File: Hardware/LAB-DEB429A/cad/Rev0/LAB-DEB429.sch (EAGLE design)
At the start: 102 parts, among them J1 TSW-132-02-S-D, J2 TSW-132-02-S-D, U1 LAB-ADSM300F, U10 SF-MICROSD, U11 25MPX, U12 LAB-PPS330D, U13 LAB-PPS330D, U14 LAB-PPS330D, U15 SI1143, U16 LAB-PPS330D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

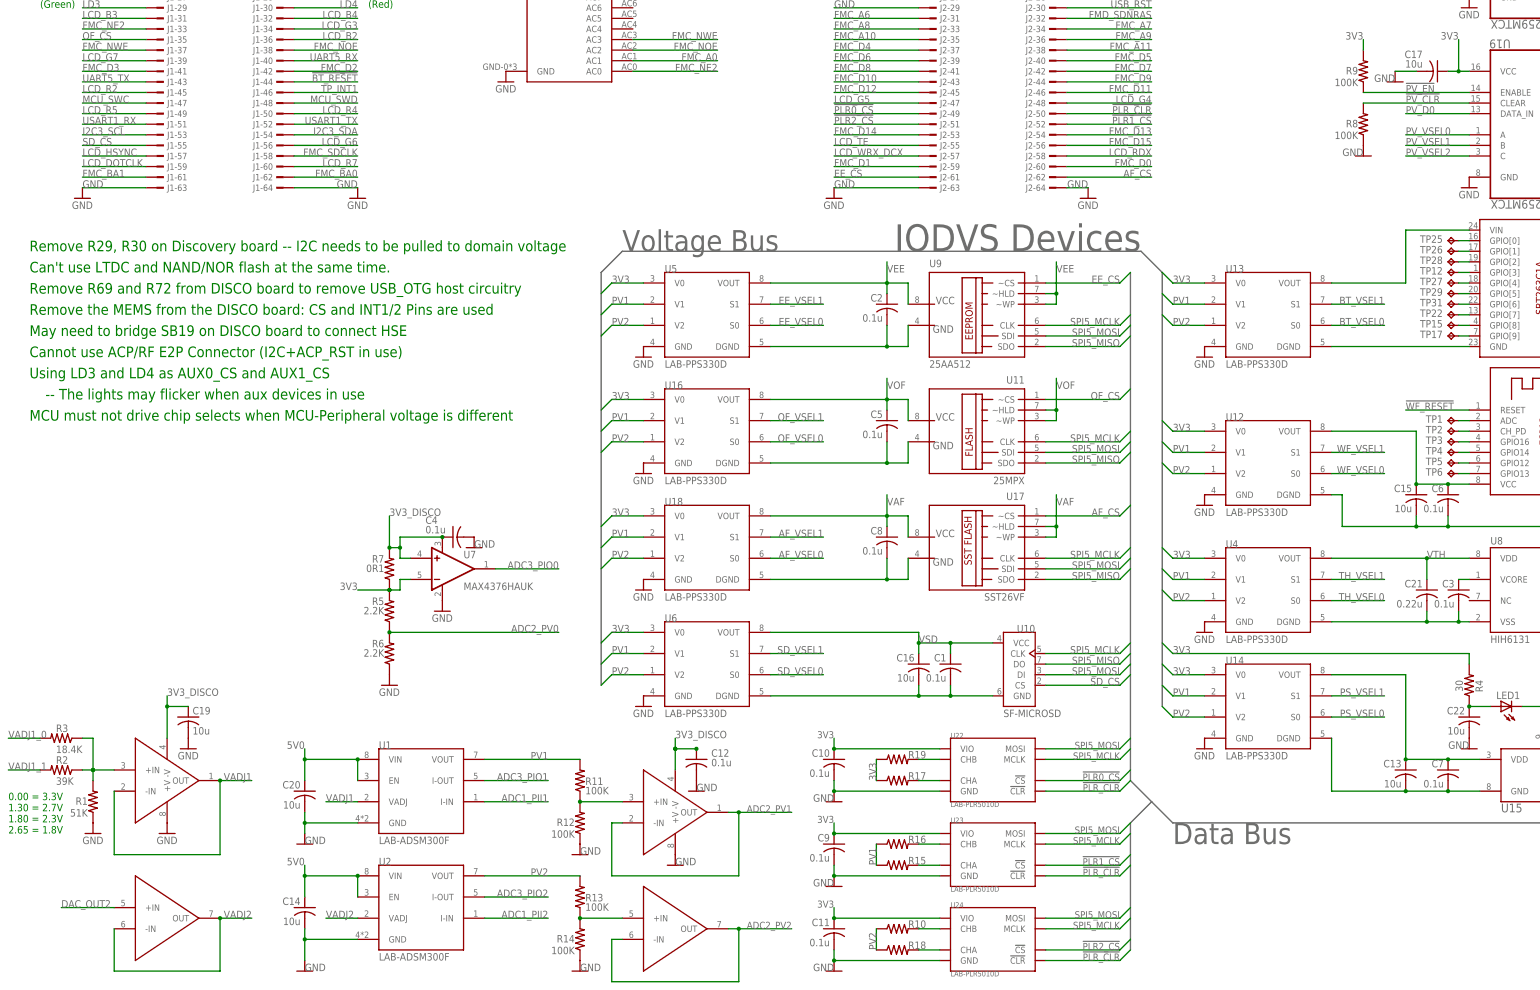
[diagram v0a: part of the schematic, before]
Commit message: 1) Updating the BOMs to synchronize purchasing.
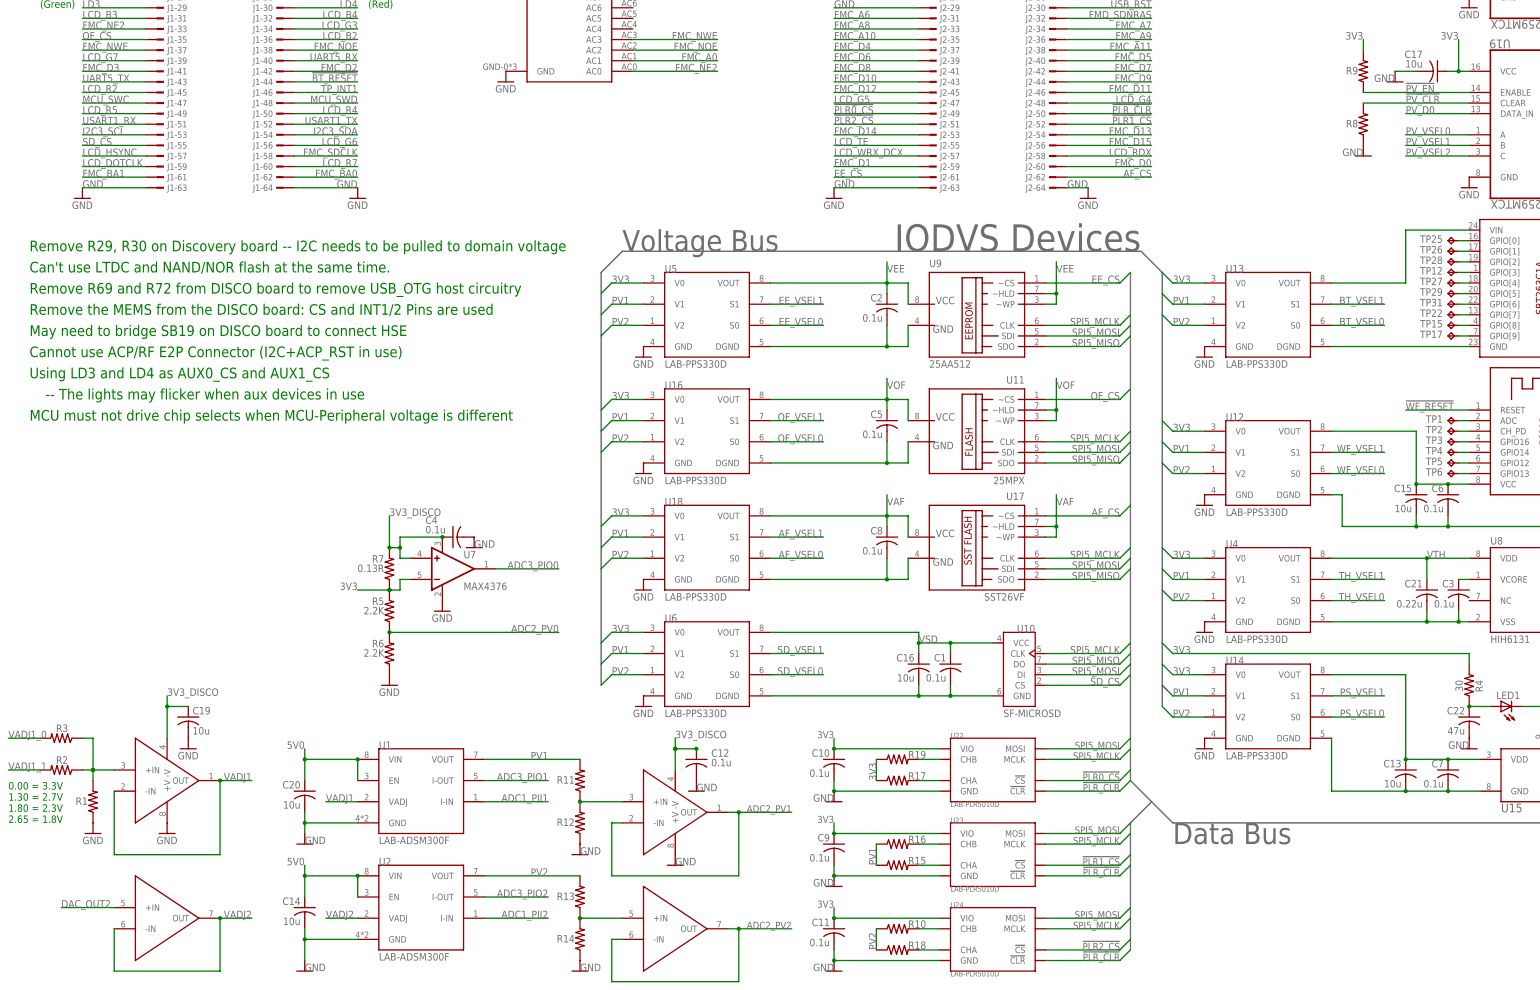
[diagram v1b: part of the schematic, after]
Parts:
- C22: value 10u -> 47u
- R1: value 51K -> (none)
- R11, R12, R13, R14, R8, R9: value 100K -> (none)
- R2: value 39K -> (none)
- R3: value 18.4K -> (none)
- R7: value 0R1 -> 0.13R
- U7: value MAX4376HAUK -> MAX4376
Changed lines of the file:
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@@
 <part name="C19" library="rcl" deviceset="C-US" device="C0603" value="10u"/>
 <part name="GND17" library="SparkFun-Aesthetics" deviceset="GND" device=""/>
-<part name="R1" library="rcl" deviceset="R-US_" device="R0603" value="51K"/>
+<part name="R1" library="rcl" deviceset="R-US_" device="R0603"/>
 <part name="GND18" library="SparkFun-Aesthetics" deviceset="GND" device=""/>
-<part name="R2" library="rcl" deviceset="R-US_" device="R0603" value="39K"/>
-<part name="R3" library="rcl" deviceset="R-US_" device="R0603" value="18.4K"/>
+<part name="R2" library="rcl" deviceset="R-US_" device="R0603"/>
+<part name="R3" library="rcl" deviceset="R-US_" device="R0603"/>
 <part name="U25" library="adafruit" deviceset="ESP-12" device=""/>
 <part name="U12" library="LAB304" deviceset="LAB-PPS330D" device=""/>
@@
 <part name="C13" library="rcl" deviceset="C-US" device="C0603" value="10u"/>
 <part name="GND2" library="SparkFun-Aesthetics" deviceset="GND" device=""/>
-<part name="C22" library="rcl" deviceset="C-US" device="C0603" value="10u"/>
+<part name="C22" library="rcl" deviceset="C-US" device="C0603" value="47u"/>
 <part name="GND3" library="SparkFun-Aesthetics" deviceset="GND" device=""/>
 <part name="U4" library="LAB304" deviceset="LAB-PPS330D" device=""/>
@@
 <part name="R6" library="rcl" deviceset="R-US_" device="R0603" value="2.2K"/>
 <part name="GND7" library="SparkFun-Aesthetics" deviceset="GND" device=""/>
-<part name="U7" library="PEGMA" deviceset="MAX4376" device="" value="MAX4376HAUK"/>
-<part name="R7" library="rcl" deviceset="R-US_" device="R0603" value="0R1"/>
+<part name="U7" library="PEGMA" deviceset="MAX4376" device=""/>
+<part name="R7" library="rcl" deviceset="R-US_" device="R0603" value="0.13R"/>
 <part name="GND8" library="SparkFun-Aesthetics" deviceset="GND" device=""/>
 <part name="C4" library="rcl" deviceset="C-US" device="C0603" value="0.1u"/>
@@
 <part name="C18" library="rcl" deviceset="C-US" device="C0603" value="10u"/>
 <part name="GND23" library="SparkFun-Aesthetics" deviceset="GND" device=""/>
-<part name="R8" library="rcl" deviceset="R-US_" device="R0603" value="100K"/>
+<part name="R8" library="rcl" deviceset="R-US_" device="R0603"/>
 <part name="GND24" library="SparkFun-Aesthetics" deviceset="GND" device=""/>
-<part name="R9" library="rcl" deviceset="R-US_" device="R0603" value="100K"/>
+<part name="R9" library="rcl" deviceset="R-US_" device="R0603"/>
 <part name="GND27" library="SparkFun-Aesthetics" deviceset="GND" device=""/>
 <part name="GND28" library="SparkFun-Aesthetics" deviceset="GND" device=""/>
@@
 <part name="C10" library="rcl" deviceset="C-US" device="C0603" value="0.1u"/>
 <part name="GND33" library="SparkFun-Aesthetics" deviceset="GND" device=""/>
-<part name="R11" library="rcl" deviceset="R-US_" device="R0603" value="100K"/>
-<part name="R12" library="rcl" deviceset="R-US_" device="R0603" value="100K"/>
-<part name="R13" library="rcl" deviceset="R-US_" device="R0603" value="100K"/>
-<part name="R14" library="rcl" deviceset="R-US_" device="R0603" value="100K"/>
+<part name="R11" library="rcl" deviceset="R-US_" device="R0603"/>
+<part name="R12" library="rcl" deviceset="R-US_" device="R0603"/>
+<part name="R13" library="rcl" deviceset="R-US_" device="R0603"/>
+<part name="R14" library="rcl" deviceset="R-US_" device="R0603"/>
 <part name="GND34" library="SparkFun-Aesthetics" deviceset="GND" device=""/>
 <part name="GND35" library="SparkFun-Aesthetics" deviceset="GND" device=""/>
@@
 <text x="10.16" y="172.72" size="2.54" layer="91">Can't use LTDC and NAND/NOR flash at the same time.</text>
 <text x="10.16" y="167.64" size="2.54" layer="91">Remove R69 and R72 from DISCO board to remove USB_OTG host circuitry</text>
-<text x="5.08" y="38.1" size="1.778" layer="91">0.00 = 3.3V
+<text x="5.08" y="40.64" size="1.778" layer="91">0.00 = 3.3V
 1.30 = 2.7V
 1.80 = 2.3V
@@
 <instance part="R1" gate="G$1" x="25.4" y="45.72" smashed="yes" rot="R90">
 <attribute name="NAME" x="24.13" y="46.7614" size="1.778" layer="95" rot="R180"/>
-<attribute name="VALUE" x="24.13" y="43.942" size="1.778" layer="96" rot="R180"/>
+<attribute name="VALUE" x="28.702" y="41.91" size="1.778" layer="96" rot="R90"/>
 </instance>
 <instance part="GND18" gate="1" x="25.4" y="38.1"/>
 <instance part="R2" gate="G$1" x="17.78" y="53.34" smashed="yes" rot="R180">
 <attribute name="NAME" x="16.51" y="54.8386" size="1.778" layer="95"/>
-<attribute name="VALUE" x="16.51" y="51.562" size="1.778" layer="96" rot="MR180"/>
+<attribute name="VALUE" x="21.59" y="56.642" size="1.778" layer="96" rot="R180"/>
 </instance>
 <instance part="R3" gate="G$1" x="17.78" y="60.96" smashed="yes" rot="R180">
 <attribute name="NAME" x="16.51" y="62.4586" size="1.778" layer="95"/>
-<attribute name="VALUE" x="16.51" y="59.182" size="1.778" layer="96" rot="MR180"/>
+<attribute name="VALUE" x="21.59" y="64.262" size="1.778" layer="96" rot="R180"/>
 </instance>
 <instance part="U25" gate="G$1" x="373.38" y="134.62"/>
@@
 <instance part="R8" gate="G$1" x="330.2" y="208.28" smashed="yes" rot="R90">
 <attribute name="NAME" x="328.93" y="209.3214" size="1.778" layer="95" rot="R180"/>
-<attribute name="VALUE" x="328.93" y="206.502" size="1.778" layer="96" rot="R180"/>
+<attribute name="VALUE" x="333.502" y="204.47" size="1.778" layer="96" rot="R90"/>
 </instance>
 <instance part="GND24" gate="1" x="330.2" y="200.66" smashed="yes">
@@
 <instance part="R9" gate="G$1" x="330.2" y="220.98" smashed="yes" rot="R90">
 <attribute name="NAME" x="328.93" y="222.0214" size="1.778" layer="95" rot="R180"/>
-<attribute name="VALUE" x="328.93" y="219.202" size="1.778" layer="96" rot="R180"/>
+<attribute name="VALUE" x="333.502" y="217.17" size="1.778" layer="96" rot="R90"/>
 </instance>
 <instance part="GND27" gate="1" x="88.9" y="190.5"/>
@@
 </instance>
 <instance part="R11" gate="G$1" x="142.24" y="50.8" smashed="yes" rot="R90">
-<attribute name="NAME" x="143.51" y="49.7586" size="1.778" layer="95"/>
-<attribute name="VALUE" x="143.51" y="47.498" size="1.778" layer="96"/>
+<attribute name="NAME" x="140.97" y="51.8414" size="1.778" layer="95" rot="R180"/>
+<attribute name="VALUE" x="145.542" y="46.99" size="1.778" layer="96" rot="R90"/>
 </instance>
 <instance part="R12" gate="G$1" x="142.24" y="40.64" smashed="yes" rot="R90">
 <attribute name="NAME" x="140.97" y="41.6814" size="1.778" layer="95" rot="R180"/>
-<attribute name="VALUE" x="140.97" y="38.862" size="1.778" layer="96" rot="R180"/>
+<attribute name="VALUE" x="145.542" y="36.83" size="1.778" layer="96" rot="R90"/>
 </instance>
 <instance part="R13" gate="G$1" x="142.24" y="22.86" smashed="yes" rot="R90">
-<attribute name="NAME" x="143.51" y="21.8186" size="1.778" layer="95"/>
-<attribute name="VALUE" x="143.51" y="19.558" size="1.778" layer="96"/>
+<attribute name="NAME" x="140.97" y="23.9014" size="1.778" layer="95" rot="R180"/>
+<attribute name="VALUE" x="145.542" y="19.05" size="1.778" layer="96" rot="R90"/>
 </instance>
 <instance part="R14" gate="G$1" x="142.24" y="12.7" smashed="yes" rot="R90">
 <attribute name="NAME" x="140.97" y="13.7414" size="1.778" layer="95" rot="R180"/>
-<attribute name="VALUE" x="140.97" y="10.922" size="1.778" layer="96" rot="R180"/>
+<attribute name="VALUE" x="145.542" y="8.89" size="1.778" layer="96" rot="R90"/>
 </instance>
 <instance part="GND34" gate="1" x="142.24" y="33.02" smashed="yes">
